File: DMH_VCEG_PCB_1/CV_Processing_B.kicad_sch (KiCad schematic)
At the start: 58 parts, among them J26 Conn_01x10_PinHeader, Q27 BC558, Q28 BC558, Q29 BC548, Q30 BC548, Q31 BC548, Q32 BC548, U18 TL074, U19 TL074, U20 TL074

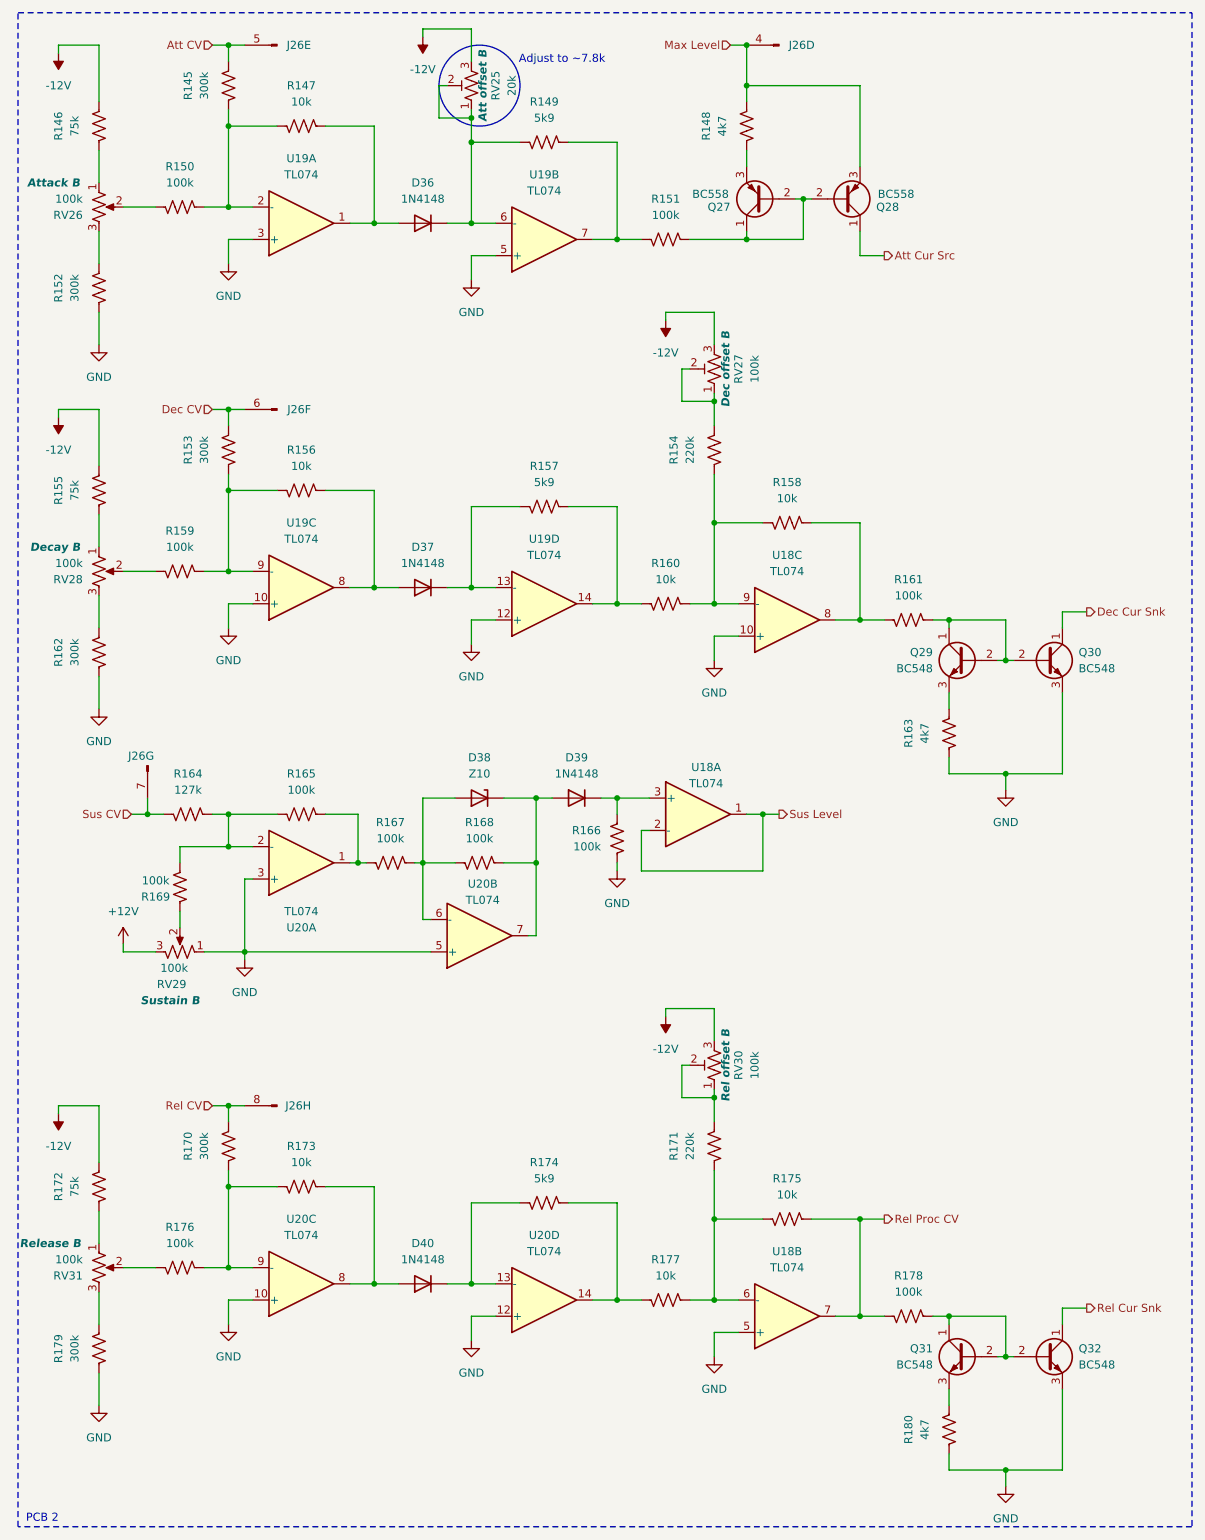
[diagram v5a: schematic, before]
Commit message: Synced PCB 2 schematic to PCB 1
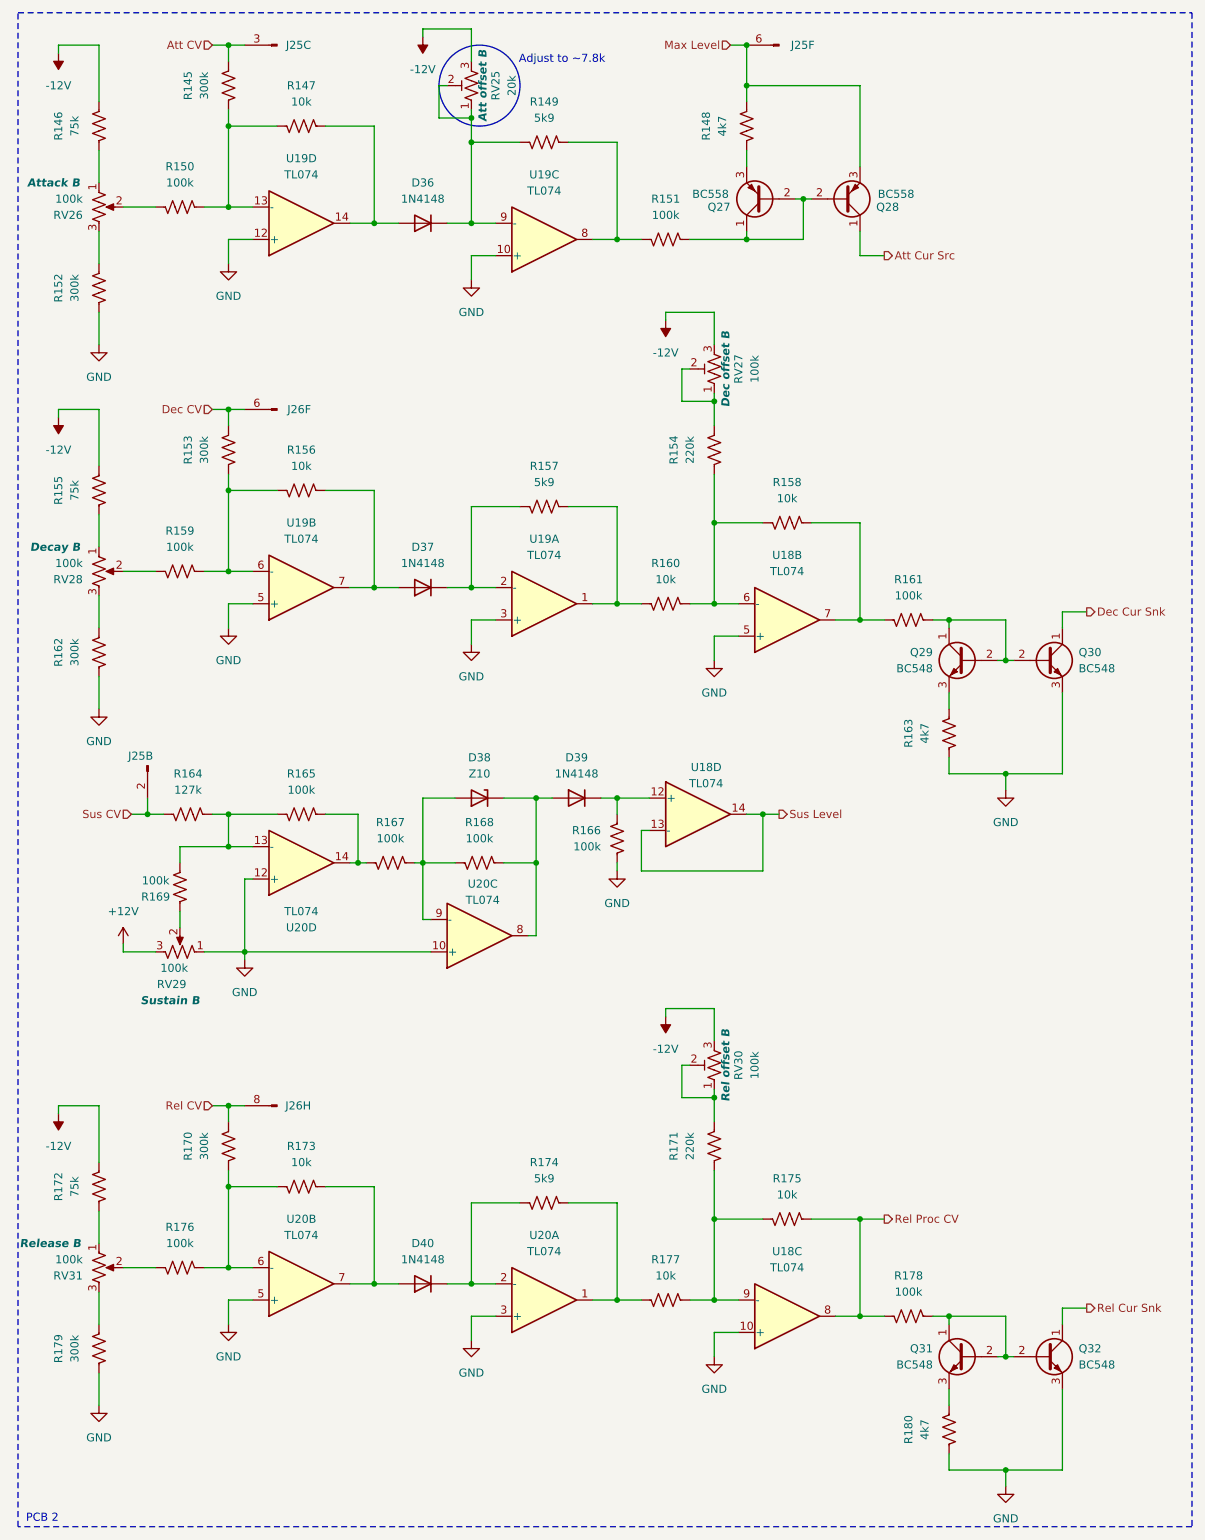
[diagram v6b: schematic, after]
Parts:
- renumbered J26 to J25
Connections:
- net Att CV: now also J25.3 (Pin_3); no longer J25.5 (Pin_5)
- net GND: now also U18.10 (+), U18.5 (+), U19.10 (+), U19.12 (+), U19.3 (+), U19.5 (+), U20.10 (+), U20.12 (+), U20.3 (+), U20.5 (+); no longer U18.10 (+), U18.5 (+), U19.10 (+), U19.12 (+), U19.3 (+), U19.5 (+), U20.10 (+), U20.12 (+), U20.3 (+), U20.5 (+)
- net Max Level: now also J25.6 (Pin_6); no longer J25.4 (Pin_4)
- net Rel Proc CV: now also U18.8; no longer U18.7
- net Sus CV: now also J25.2 (Pin_2); no longer J25.7 (Pin_7)
- net Sus Level: now also U18.13 (-), U18.14; no longer U18.1, U18.2 (-)
- net at D37.1 (K), R157.1: now also U19.2 (-); no longer U19.13 (-)
- net at R157.2, R160.1: now also U19.1; no longer U19.14
- net at R145.1, R147.1, R150.2: now also U19.13 (-); no longer U19.2 (-)
- net at R170.1, R173.1, R176.2: now also U20.6 (-); no longer U20.9 (-)
- net at R165.2, R167.1: now also U20.14; no longer U20.1
- net at D38.2 (A), R167.2, R168.1: now also U20.9 (-); no longer U20.6 (-)
- net at D36.2 (A), R147.2: now also U19.14; no longer U19.1
- net at R149.2, R151.1: now also U19.8; no longer U19.7
- net at R153.1, R156.1, R159.2: now also U19.6 (-); no longer U19.9 (-)
- net at D39.1 (K), R166.2: now also U18.12 (+); no longer U18.3 (+)
- net at R171.1, R175.1, R177.2: now also U18.9 (-); no longer U18.6 (-)
- net at D36.1 (K), R149.1, RV25.1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: now also U19.9 (-); no longer U19.6 (-)
- net at D38.1 (K), D39.2 (A), R168.2: now also U20.8; no longer U20.7
- net at D40.2 (A), R173.2: now also U20.7; no longer U20.8
- net at R158.2, R161.1: now also U18.7; no longer U18.8
- net at D40.1 (K), R174.1: now also U20.2 (-); no longer U20.13 (-)
- net at R174.2, R177.1: now also U20.1; no longer U20.14
- net at D37.2 (A), R156.2: now also U19.7; no longer U19.8
- net at R164.2, R165.1, R169.2: now also U20.13 (-); no longer U20.2 (-)
- net at R154.1, R158.1, R160.2: now also U18.6 (-); no longer U18.9 (-)
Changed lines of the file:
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@@
 		)
 	)
+	(netclass_flag ""
+		(length 2.54)
+		(shape round)
+		(at 45.72 185.42 0)
+		(fields_autoplaced yes)
+		(effects
+			(font
+				(size 1.27 1.27)
+			)
+			(justify left bottom)
+		)
+		(property "Netclass" "CrossPCB"
+			(at 46.4185 182.88 0)
+			(effects
+				(font
+					(size 1.27 1.27)
+				)
+				(justify left)
+				(hide yes)
+			)
+		)
+		(property "Component Class" ""
+			(at -129.54 177.8 0)
+			(effects
+				(font
+					(size 1.27 1.27)
+					(italic yes)
+				)
+			)
+		)
+	)
+	(netclass_flag ""
+		(length 2.54)
+		(shape round)
+		(at 127 19.05 0)
+		(fields_autoplaced yes)
+		(effects
+			(font
+				(size 1.27 1.27)
+			)
+			(justify left bottom)
+		)
+		(property "Netclass" "CrossPCB"
+			(at 127.6985 16.51 0)
+			(effects
+				(font
+					(size 1.27 1.27)
+				)
+				(justify left)
+				(hide yes)
+			)
+		)
+		(property "Component Class" ""
+			(at -48.26 11.43 0)
+			(effects
+				(font
+					(size 1.27 1.27)
+					(italic yes)
+				)
+			)
+		)
+	)
+	(netclass_flag ""
+		(length 2.54)
+		(shape round)
+		(at 45.72 76.2 0)
+		(fields_autoplaced yes)
+		(effects
+			(font
+				(size 1.27 1.27)
+			)
+			(justify left bottom)
+		)
+		(property "Netclass" "CrossPCB"
+			(at 46.4185 73.66 0)
+			(effects
+				(font
+					(size 1.27 1.27)
+				)
+				(justify left)
+				(hide yes)
+			)
+		)
+		(property "Component Class" ""
+			(at -129.54 68.58 0)
+			(effects
+				(font
+					(size 1.27 1.27)
+					(italic yes)
+				)
+			)
+		)
+	)
+	(netclass_flag ""
+		(length 2.54)
+		(shape round)
+		(at 45.72 19.05 0)
+		(fields_autoplaced yes)
+		(effects
+			(font
+				(size 1.27 1.27)
+			)
+			(justify left bottom)
+		)
+		(property "Netclass" "CrossPCB"
+			(at 46.4185 16.51 0)
+			(effects
+				(font
+					(size 1.27 1.27)
+				)
+				(justify left)
+				(hide yes)
+			)
+		)
+		(property "Component Class" ""
+			(at -129.54 11.43 0)
+			(effects
+				(font
+					(size 1.27 1.27)
+					(italic yes)
+				)
+			)
+		)
+	)
+	(netclass_flag ""
+		(length 2.54)
+		(shape round)
+		(at 33.02 139.7 180)
+		(fields_autoplaced yes)
+		(effects
+			(font
+				(size 1.27 1.27)
+			)
+			(justify right bottom)
+		)
+		(property "Netclass" "CrossPCB"
+			(at 33.7185 142.24 0)
+			(effects
+				(font
+					(size 1.27 1.27)
+				)
+				(justify left)
+				(hide yes)
+			)
+		)
+		(property "Component Class" ""
+			(at -142.24 132.08 0)
+			(effects
+				(font
+					(size 1.27 1.27)
+					(italic yes)
+				)
+			)
+		)
+	)
 	(symbol
 		(lib_id "Device:R_US")
@@
 		(lib_id "Amplifier_Operational:TL074")
 		(at 119.38 139.7 0)
-		(unit 1)
+		(unit 4)
 		(exclude_from_sim no)
 		(in_bom yes)
@@
 				(path "/58f4306d-5387-4983-bb08-41a2313fd315/b3f92c0e-ea97-4ef0-9a6b-254feed98ad2"
 					(reference "U18")
-					(unit 1)
+					(unit 4)
 				)
 			)
@@
 		(lib_id "SynthStuff:Conn_01x10_PinHeader")
 		(at 33.02 132.08 270)
-		(unit 7)
+		(unit 2)
 		(exclude_from_sim no)
 		(in_bom yes)
 		(on_board yes)
 		(dnp no)
-		(property "Reference" "J26"
+		(property "Reference" "J25"
 			(at 29.972 130.556 90)
 			(effects
@@
 			(project "DMH_VCEG_PCB_1"
 				(path "/58f4306d-5387-4983-bb08-41a2313fd315/b3f92c0e-ea97-4ef0-9a6b-254feed98ad2"
-					(reference "J26")
-					(unit 7)
+					(reference "J25")
+					(unit 2)
 				)
 			)
@@
 		(at 133.35 218.44 0)
 		(mirror x)
-		(unit 2)
+		(unit 3)
 		(exclude_from_sim no)
 		(in_bom yes)
@@
 				(path "/58f4306d-5387-4983-bb08-41a2313fd315/b3f92c0e-ea97-4ef0-9a6b-254feed98ad2"
 					(reference "U18")
-					(unit 2)
+					(unit 3)
 				)
 			)
@@
 		(at 95.25 49.53 0)
 		(mirror x)
-		(unit 2)
+		(unit 3)
 		(exclude_from_sim no)
 		(in_bom yes)
@@
 				(path "/58f4306d-5387-4983-bb08-41a2313fd315/b3f92c0e-ea97-4ef0-9a6b-254feed98ad2"
 					(reference "U19")
-					(unit 2)
+					(unit 3)
 				)
 			)
@@
 		(at 57.15 213.36 0)
 		(mirror x)
-		(unit 3)
+		(unit 2)
 		(exclude_from_sim no)
 		(in_bom yes)
@@
 				(path "/58f4306d-5387-4983-bb08-41a2313fd315/b3f92c0e-ea97-4ef0-9a6b-254feed98ad2"
 					(reference "U20")
-					(unit 3)
+					(unit 2)
 				)
 			)
@@
 		(at 95.25 215.9 0)
 		(mirror x)
-		(unit 4)
+		(unit 1)
 		(exclude_from_sim no)
 		(in_bom yes)
@@
 				(path "/58f4306d-5387-4983-bb08-41a2313fd315/b3f92c0e-ea97-4ef0-9a6b-254feed98ad2"
 					(reference "U20")
-					(unit 4)
+					(unit 1)
 				)
 			)
@@
 		(lib_id "SynthStuff:Conn_01x10_PinHeader")
 		(at 53.34 19.05 180)
-		(unit 5)
+		(unit 3)
 		(exclude_from_sim no)
 		(in_bom yes)
 		(on_board yes)
 		(dnp no)
-		(property "Reference" "J26"
+		(property "Reference" "J25"
 			(at 58.674 19.05 0)
 			(effects
@@
 			(project "DMH_VCEG_PCB_1"
 				(path "/58f4306d-5387-4983-bb08-41a2313fd315/b3f92c0e-ea97-4ef0-9a6b-254feed98ad2"
-					(reference "J26")
-					(unit 5)
+					(reference "J25")
+					(unit 3)
 				)
 			)
@@
 		(at 85.09 158.75 0)
 		(mirror x)
-		(unit 2)
+		(unit 3)
 		(exclude_from_sim no)
 		(in_bom yes)
@@
 				(path "/58f4306d-5387-4983-bb08-41a2313fd315/b3f92c0e-ea97-4ef0-9a6b-254feed98ad2"
 					(reference "U20")
-					(unit 2)
+					(unit 3)
 				)
 			)
@@
 		(lib_id "SynthStuff:Conn_01x10_PinHeader")
 		(at 132.08 19.05 180)
-		(unit 4)
+		(unit 6)
 		(exclude_from_sim no)
 		(in_bom yes)
 		(on_board yes)
 		(dnp no)
-		(property "Reference" "J26"
+		(property "Reference" "J25"
 			(at 137.668 19.05 0)
 			(effects
@@
 			(project "DMH_VCEG_PCB_1"
 				(path "/58f4306d-5387-4983-bb08-41a2313fd315/b3f92c0e-ea97-4ef0-9a6b-254feed98ad2"
-					(reference "J26")
-					(unit 4)
+					(reference "J25")
+					(unit 6)
 				)
 			)
@@
 		(at 57.15 46.99 0)
 		(mirror x)
-		(unit 1)
+		(unit 4)
 		(exclude_from_sim no)
 		(in_bom yes)
@@
 				(path "/58f4306d-5387-4983-bb08-41a2313fd315/b3f92c0e-ea97-4ef0-9a6b-254feed98ad2"
 					(reference "U19")
-					(unit 1)
+					(unit 4)
 				)
 			)
@@
 		(at 57.15 104.14 0)
 		(mirror x)
-		(unit 3)
+		(unit 2)
 		(exclude_from_sim no)
 		(in_bom yes)
@@
 				(path "/58f4306d-5387-4983-bb08-41a2313fd315/b3f92c0e-ea97-4ef0-9a6b-254feed98ad2"
 					(reference "U19")
-					(unit 3)
+					(unit 2)
 				)
 			)
@@
 		(at 133.35 109.22 0)
 		(mirror x)
-		(unit 3)
+		(unit 2)
 		(exclude_from_sim no)
 		(in_bom yes)
@@
 				(path "/58f4306d-5387-4983-bb08-41a2313fd315/b3f92c0e-ea97-4ef0-9a6b-254feed98ad2"
 					(reference "U18")
-					(unit 3)
+					(unit 2)
 				)
 			)
@@
 		(at 95.25 106.68 0)
 		(mirror x)
-		(unit 4)
+		(unit 1)
 		(exclude_from_sim no)
 		(in_bom yes)
@@
 				(path "/58f4306d-5387-4983-bb08-41a2313fd315/b3f92c0e-ea97-4ef0-9a6b-254feed98ad2"
 					(reference "U19")
-					(unit 4)
+					(unit 1)
 				)
 			)
@@
 		(at 57.15 147.32 0)
 		(mirror x)
-		(unit 1)
+		(unit 4)
 		(exclude_from_sim no)
 		(in_bom yes)
@@
 				(path "/58f4306d-5387-4983-bb08-41a2313fd315/b3f92c0e-ea97-4ef0-9a6b-254feed98ad2"
 					(reference "U20")
-					(unit 1)
+					(unit 4)
 				)
 			)

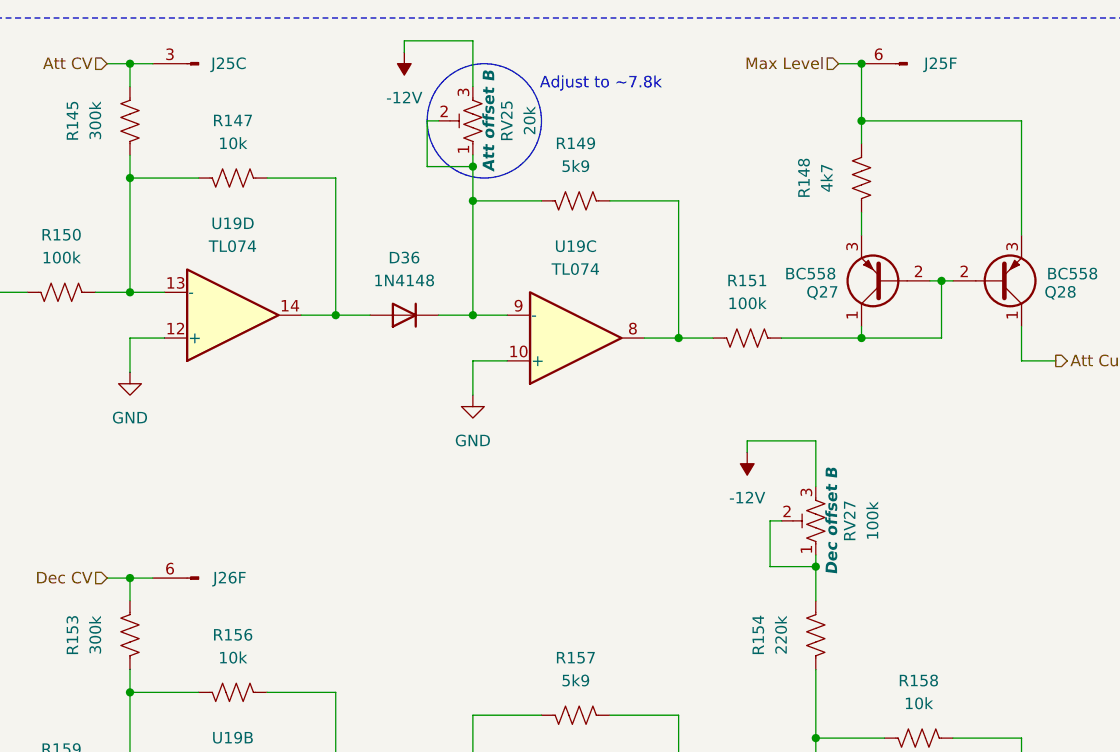
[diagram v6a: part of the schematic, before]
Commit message: PCB 1 placement in progress
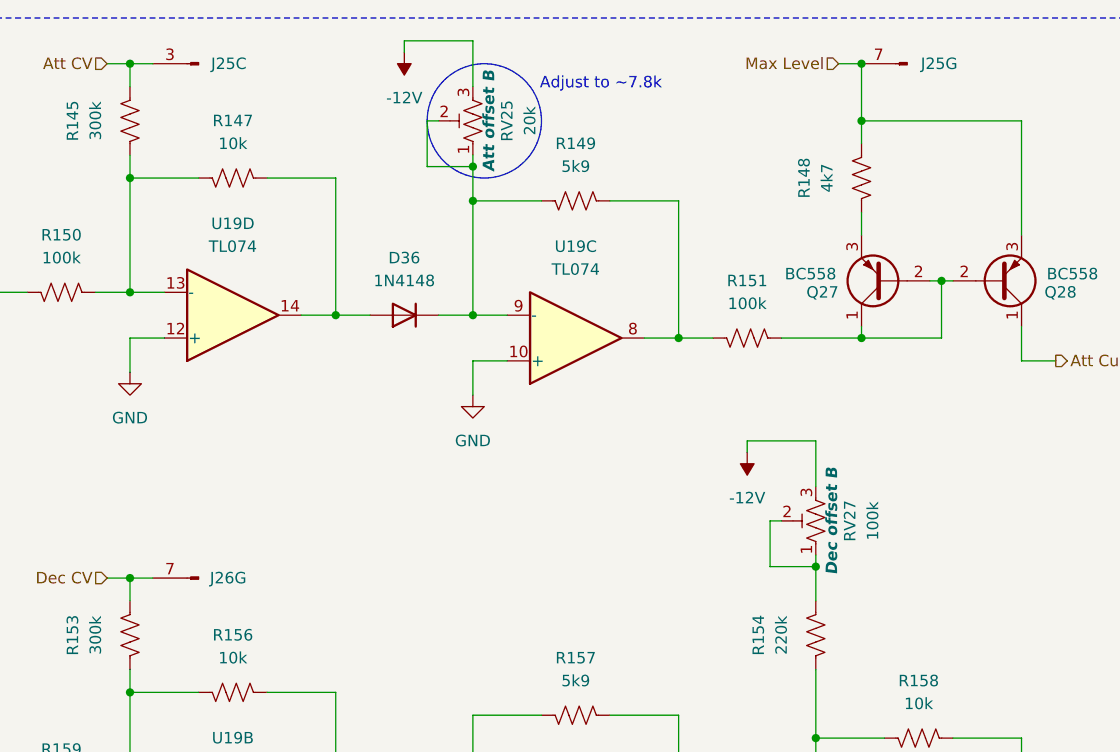
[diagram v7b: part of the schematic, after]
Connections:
- net Dec CV: now also J26.7 (Pin_7); no longer J26.6 (Pin_6)
- net Max Level: now also J25.7 (Pin_7); no longer J25.6 (Pin_6)
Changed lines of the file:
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@@
 		(lib_id "SynthStuff:Conn_01x10_PinHeader")
 		(at 53.34 76.2 180)
-		(unit 6)
+		(unit 7)
 		(exclude_from_sim no)
 		(in_bom yes)
@@
 				(path "/58f4306d-5387-4983-bb08-41a2313fd315/b3f92c0e-ea97-4ef0-9a6b-254feed98ad2"
 					(reference "J26")
-					(unit 6)
+					(unit 7)
 				)
 			)
@@
 		(lib_id "SynthStuff:Conn_01x10_PinHeader")
 		(at 132.08 19.05 180)
-		(unit 6)
+		(unit 7)
 		(exclude_from_sim no)
 		(in_bom yes)
@@
 				(path "/58f4306d-5387-4983-bb08-41a2313fd315/b3f92c0e-ea97-4ef0-9a6b-254feed98ad2"
 					(reference "J25")
-					(unit 6)
-				)
-			)
+					(unit 7)
+				)
+			)
